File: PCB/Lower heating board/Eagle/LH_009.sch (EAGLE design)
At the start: 8 parts, among them X1 MKDSN1,5/4-5,08

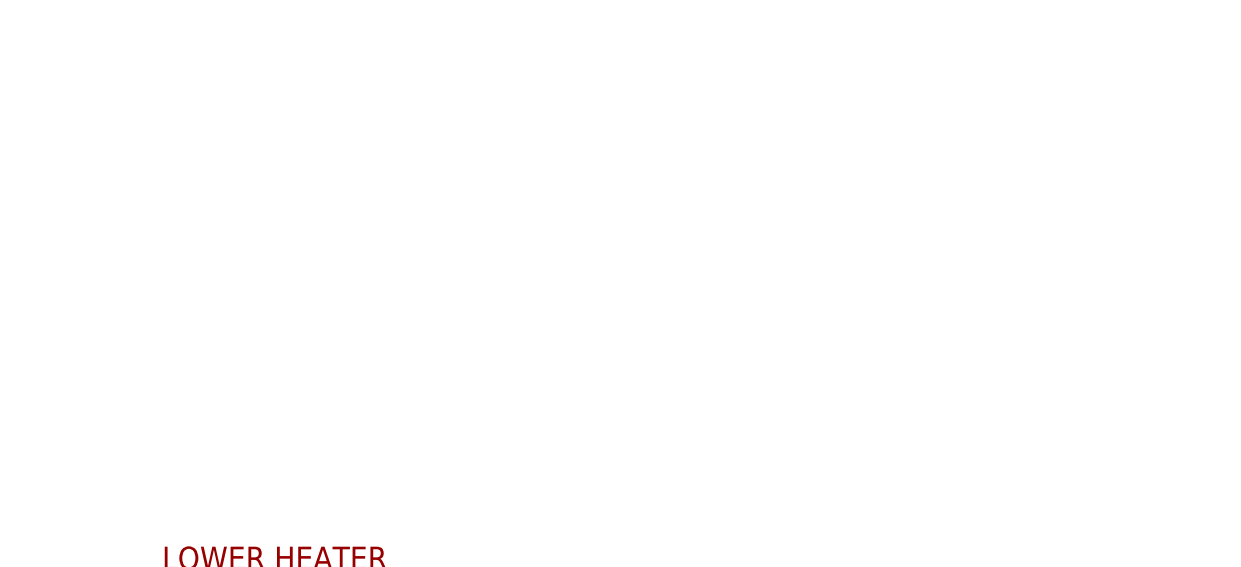
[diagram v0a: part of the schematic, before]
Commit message: PCB modification, CERN license
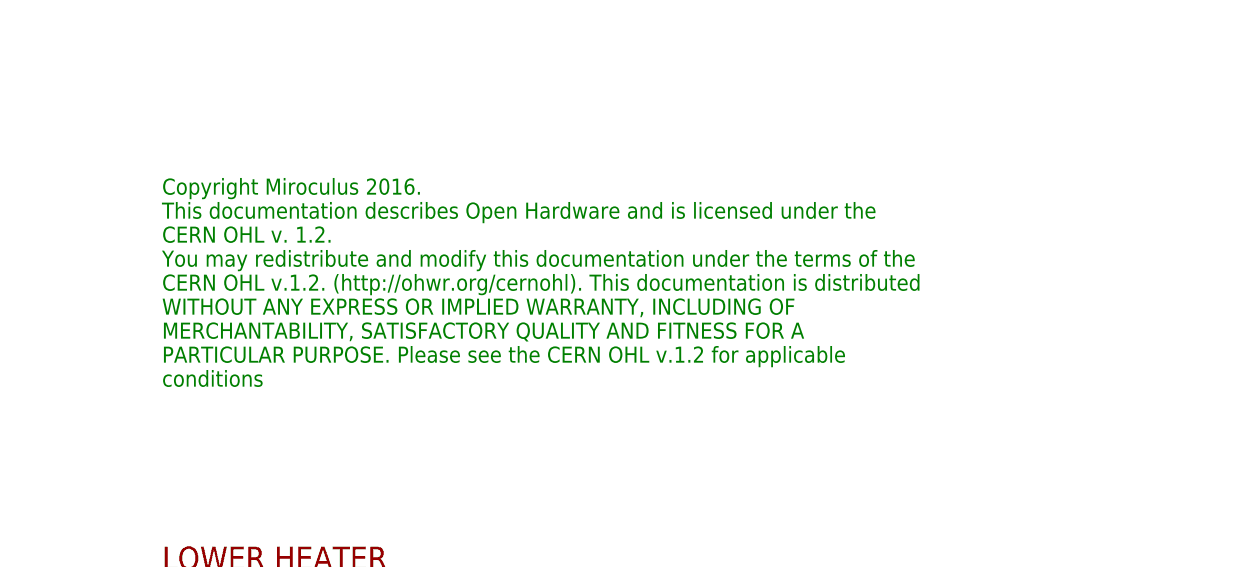
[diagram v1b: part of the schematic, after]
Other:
- note added: "Copyright Miroculus 2016. This documentation describes Open Hardware and is licensed under the CERN OHL v. 1.2. You may redistribute and modify this documentation under the terms of the CERN OHL v.1.2. (http://ohwr.org/cernohl). This documentation is distributed WITHOUT ANY EXPRESS OR IMPLIED WARRANTY, INCLUDING OF MERCHANTABILITY, SATISFACTORY QUALITY AND FITNESS FOR A PARTICULAR PURPOSE. Please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"
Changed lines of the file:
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@@
 <wire x1="-236.22" y1="220.98" x2="-243.84" y2="220.98" width="0.1524" layer="94"/>
 <wire x1="-243.84" y1="220.98" x2="-243.84" y2="241.3" width="0.1524" layer="94"/>
+<text x="-99.06" y="124.46" size="1.778" layer="91">Copyright Miroculus 2016.
+This documentation describes Open Hardware and is licensed under the
+CERN OHL v. 1.2.
+You may redistribute and modify this documentation under the terms of the
+CERN OHL v.1.2. (http://ohwr.org/cernohl). This documentation is distributed
+WITHOUT ANY EXPRESS OR IMPLIED WARRANTY, INCLUDING OF
+MERCHANTABILITY, SATISFACTORY QUALITY AND FITNESS FOR A
+PARTICULAR PURPOSE. Please see the CERN OHL v.1.2 for applicable
+conditions</text>
 </plain>
 <instances>
